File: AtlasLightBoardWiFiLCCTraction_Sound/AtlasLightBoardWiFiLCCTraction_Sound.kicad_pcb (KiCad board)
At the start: 2 copper layers, 76.7 x 20.3 mm, 47 parts, among them IC102 MP6614GN-Z, J101 USB_C_Receptacle, SW101 Reset, SW102 Boot, U101 ESP32_S3_WROOM, U102 TBD62083A, U103 AP63203WU

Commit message: Added I2S => Speaker chip (MAX98357A).
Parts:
- added TP105: Speaker, TestPoint:TestPoint_2Pads_Pitch2.54mm_Drill0.8mm, F.Cu at (133.4, 82.1)
- added U104: MAX98357AETE+T, Package_DFN_QFN:TQFN-16-1EP_3x3mm_P0.5mm_EP1.23x1.23mm_ThermalVias, F.Cu at (133.4, 78.7)
- moved U101 6.00 mm to (147.1, 78.7)
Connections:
- U101 pad 19: unconnected-(U101-Pad19) -> /I2S_TX
- U101 pad 20: unconnected-(U101-Pad20) -> /I2S_BCLK
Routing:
- net /I2S_TX: track 0.00 -> 7.90 mm, vias 0 -> 2
- net /D-: track 25.5 -> 33.3 mm
- net /D+: track 26.0 -> 33.7 mm
- net /Function2: track 73.9 -> 81.0 mm
- net /I2S_BCLK: track 0.00 -> 6.91 mm, vias 0 -> 2
- net +3V3: track 93.4 -> 99.8 mm
- net /Function3: track 75.0 -> 81.4 mm
- net /Reset: track 29.1 -> 35.4 mm
- net /MForward: track 54.6 -> 60.8 mm
- net /Function4: track 76.3 -> 82.4 mm
- net /MReverse: track 52.4 -> 58.4 mm
- net /Function5: track 74.3 -> 80.1 mm
- net GND: track 120.3 -> 126.0 mm
- net /Function6: track 87.6 -> 93.3 mm
- net Net-(TP105-Pad2): track 0.00 -> 3.79 mm
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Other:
- board size 76.7 x 20.3 mm -> 82.7 x 20.3 mm

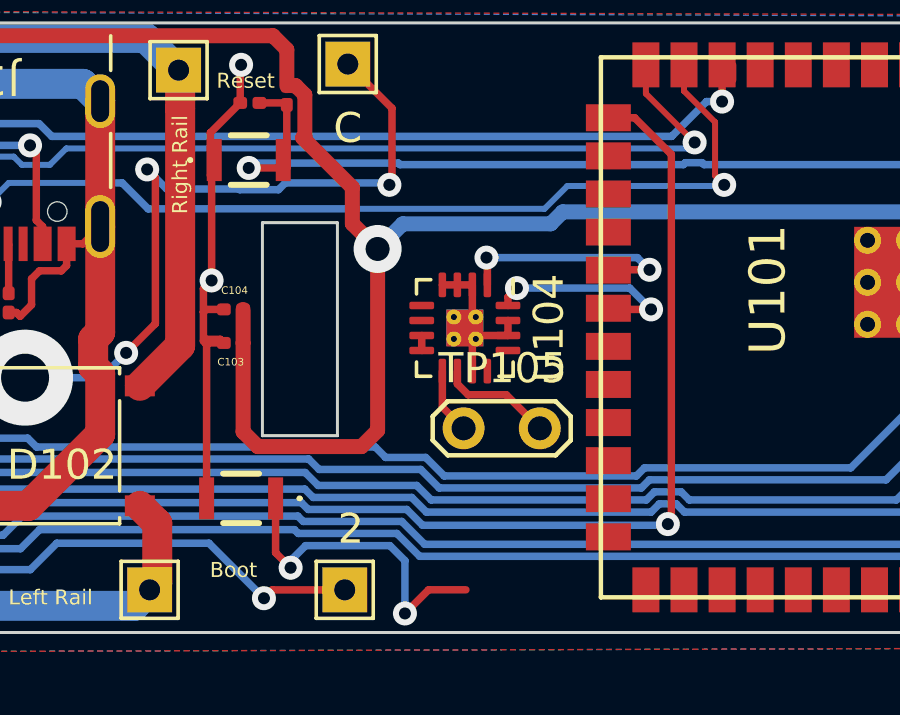
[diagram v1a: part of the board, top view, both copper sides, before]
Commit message: Added I2S => Speaker chip (MAX98357A).
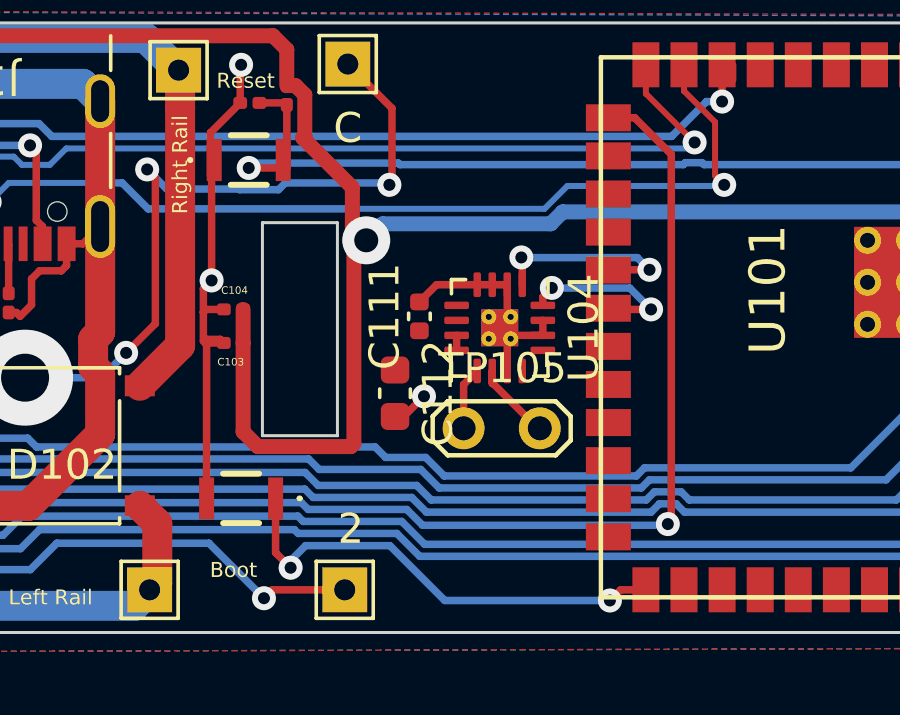
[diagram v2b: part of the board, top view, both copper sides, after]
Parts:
- added C111: .1uf, Capacitor_SMD:C_0402_1005Metric, F.Cu at (131.9, 78.4)
- added C112: 10 uf 6.3V, Capacitor_SMD:C_0603_1608Metric, F.Cu at (131.1, 80.9)
- moved U104 1.16 mm to (134.6, 78.7)
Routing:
- net /Boot0: track 11.1 -> 15.7 mm
- net GND: track 126.0 -> 129.4 mm, vias 5 -> 6
- net /I2S_TX: track 7.90 -> 6.74 mm
- net /I2S_BCLK: track 6.91 -> 5.75 mm
- net Net-(TP105-Pad2): track 3.79 -> 3.03 mm

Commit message: Update the doc/Images files.
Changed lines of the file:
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@@
     (property "Sheetname" "")
     (attr exclude_from_pos_files)
-    (fp_text reference "TP105" (at 1.3 -2) (layer "F.SilkS")
-      (effects (font (size 1 1) (thickness 0.15)))
-    )
-    (fp_text value "Speaker" (at 1.27 2) (layer "F.Fab")
+    (fp_text reference "TP105" (at 1.3 -2) (layer "F.Fab")
+      (effects (font (size 1 1) (thickness 0.15)))
+    )
+    (fp_text value "Speaker" (at 0.3556 1.9812) (layer "F.SilkS")
       (effects (font (size 1 1) (thickness 0.15)))
     )
@@
     (property "Sheetname" "")
     (attr smd)
-    (fp_text reference "C111" (at 0 -1.16 90) (layer "F.SilkS")
-      (effects (font (size 1 1) (thickness 0.15)))
+    (fp_text reference "C111" (at 0.0788 -0.9652 90) (layer "F.SilkS")
+      (effects (font (size 0.5 0.5) (thickness 0.075)))
     )
     (fp_text value ".1uf" (at 0 1.16 90) (layer "F.Fab")
@@
     (property "Sheetname" "")
     (attr smd)
-    (fp_text reference "C112" (at 0 -1.43 90) (layer "F.SilkS")
-      (effects (font (size 1 1) (thickness 0.15)))
+    (fp_text reference "C112" (at 0.254 1.2192 90) (layer "F.SilkS")
+      (effects (font (size 0.5 0.5) (thickness 0.075)))
     )
     (fp_text value "10 uf 6.3V" (at 0 1.43 90) (layer "F.Fab")
@@
     (property "Value_1" "MAX98357AETE+T")
     (attr smd)
-    (fp_text reference "U104" (at 0 -2.8 90) (layer "F.SilkS")
-      (effects (font (size 1 1) (thickness 0.15)))
+    (fp_text reference "U104" (at -0.258 -2.5043 90) (layer "F.SilkS")
+      (effects (font (size 0.5 0.5) (thickness 0.075)))
     )
     (fp_text value "MAX98357AETE+T" (at 0 2.8 90) (layer "F.Fab")
@@
     (pad "17" thru_hole circle (at -0.365 0.365 270) (size 0.5 0.5) (drill 0.2) (layers *.Cu)
       (net 2 "GND") (pinfunction "THERMAL_PAD") (pintype "passive"))
-    (model "${KICAD6_3DMODEL_DIR}/Package_DFN_QFN.3dshapes/TQFN-16-1EP_3x3mm_P0.5mm_EP1.23x1.23mm.wrl"
-      (offset (xyz 0 0 0))
-      (scale (xyz 1 1 1))
+    (model "${KICAD6_3DMODEL_DIR}/Package_DFN_QFN.3dshapes/QFN-16-1EP_3x3mm_P0.5mm_EP1.8x1.8mm.step"
+      (offset (xyz 0 0 0))
+      (scale (xyz 1 1 1))

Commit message: Add WS / LR Clock.
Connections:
- U101 pad 21: unconnected-(U101-Pad21) -> /LRCLK
- U104 pad 14: GND -> /LRCLK
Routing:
- net /LRCLK: track 0.00 -> 2.34 mm
- net GND: track 129.4 -> 128.8 mm
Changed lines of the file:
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@@
   (net 49 "Net-(TP105-Pad1)")
   (net 50 "Net-(TP105-Pad2)")
-  (net 51 "unconnected-(U101-Pad21)")
+  (net 51 "/LRCLK")
   (net 52 "unconnected-(U101-Pad22)")
   (net 53 "unconnected-(U101-Pad23)")
@@
       (net 71 "/I2S_BCLK") (pinfunction "IO12") (pintype "bidirectional"))
     (pad "21" smd rect locked (at 0.635 8.87 270) (size 0.9 1.5) (layers "F.Cu" "F.Paste" "F.Mask")
-      (net 51 "unconnected-(U101-Pad21)") (pinfunction "IO13") (pintype "bidirectional+no_connect"))
+      (net 51 "/LRCLK") (pinfunction "IO13") (pintype "bidirectional"))
     (pad "22" smd rect locked (at 1.905 8.87 270) (size 0.9 1.5) (layers "F.Cu" "F.Paste" "F.Mask")
       (net 52 "unconnected-(U101-Pad22)") (pinfunction "IO14") (pintype "bidirectional+no_connect"))
@@
       (net 76 "unconnected-(U104-Pad13)") (pinfunction "N.C._4") (pintype "passive+no_connect"))
     (pad "14" smd roundrect (at 0.25 -1.4375 270) (size 0.25 0.825) (layers "F.Cu" "F.Paste" "F.Mask") (roundrect_rratio 0.25)
-      (net 2 "GND") (pinfunction "LRCLK") (pintype "passive"))
+      (net 51 "/LRCLK") (pinfunction "LRCLK") (pintype "passive"))
     (pad "15" smd roundrect (at -0.25 -1.4375 270) (size 0.25 0.825) (layers "F.Cu" "F.Paste" "F.Mask") (roundrect_rratio 0.25)
       (net 2 "GND") (pinfunction "GND_3") (pintype "passive"))
@@
   (segment (start 121.052287 80.03442) (end 121.287 80.269133) (width 1) (layer "F.Cu") (net 2))
   (segment (start 103.403 74.168) (end 103.378 74.168) (width 0.25) (layer "F.Cu") (net 2))
-  (segment (start 136.0424 78.994) (end 134.8549 78.994) (width 0.25) (layer "F.Cu") (net 2))
   (segment (start 107.569 77.535) (end 107.442 77.662) (width 0.25) (layer "F.Cu") (net 2))
-  (segment (start 136.0424 78.494) (end 136.0424 78.994) (width 0.25) (layer "F.Cu") (net 2))
   (segment (start 131.4066 81.6994) (end 132.08 81.026) (width 0.25) (layer "F.Cu") (net 2))
   (segment (start 124.834 79.128) (end 125.29 79.128) (width 0.25) (layer "F.Cu") (net 2))
@@
   (segment (start 92.362 80.805) (end 92.329 80.772) (width 0.25) (layer "F.Cu") (net 2))
   (segment (start 118.999 77.978) (end 118.999 77.111) (width 0.25) (layer "F.Cu") (net 2))
+  (segment (start 135.0849 78.494) (end 134.9699 78.379) (width 0.25) (layer "F.Cu") (net 2))
   (segment (start 108.585 76.454) (end 106.68 78.359) (width 0.25) (layer "F.Cu") (net 2))
   (segment (start 124.8156 78.1304) (end 124.727 78.219) (width 0.25) (layer "F.Cu") (net 2))
   (segment (start 133.8549 77.3065) (end 134.3549 77.3065) (width 0.25) (layer "F.Cu") (net 2))
+  (segment (start 136.0424 78.494) (end 135.0849 78.494) (width 0.25) (layer "F.Cu") (net 2))
   (segment (start 113.767 75.943) (end 113.222 75.943) (width 0.25) (layer "F.Cu") (net 2))
   (segment (start 119.267 76.843) (end 119.992 76.843) (width 0.25) (layer "F.Cu") (net 2))
@@
   (segment (start 134.3549 80.1815) (end 134.3549 80.6088) (width 0.25) (layer "F.Cu") (net 50))
   (segment (start 135.876403 82.0928) (end 135.9408 82.0928) (width 0.25) (layer "F.Cu") (net 50))
+  (segment (start 136.0424 78.994) (end 137.859 78.994) (width 0.25) (layer "F.Cu") (net 51))
+  (segment (start 137.859 78.994) (end 138.227 79.362) (width 0.25) (layer "F.Cu") (net 51))
   (segment (start 92.5068 73.751101) (end 92.5068 73.688) (width 0.25) (layer "F.Cu") (net 69))
   (segment (start 91.643 75.847) (end 91.643 74.614901) (width 0.25) (layer "F.Cu") (net 69))

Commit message: Minor tweaks: MONO mode resister, trace symblification.
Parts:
- added R111: 634k, Resistor_SMD:R_0402_1005Metric, F.Cu at (133.3, 76.0)
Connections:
- U104 pad 4: GND -> Net-(U104-Pad4)
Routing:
- net /I2S_TX: track 6.74 -> 3.09 mm, vias 2 -> 0
- net /I2S_BCLK: track 5.75 -> 2.28 mm, vias 2 -> 0
- net GND: track 128.8 -> 127.1 mm, vias 6 -> 7
- net Net-(U104-Pad4): track 0.00 -> 1.33 mm
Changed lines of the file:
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@@
   (net 75 "unconnected-(U104-Pad12)")
   (net 76 "unconnected-(U104-Pad13)")
+  (net 77 "Net-(U104-Pad4)")
   (footprint "TestPoint:TestPoint_THTPad_1.5x1.5mm_Drill0.7mm" (layer "F.Cu")
     (at 122.936 87.4776)
@@
       (net 21 "Net-(R103-Pad1)") (pinfunction "1") (pintype "passive"))
   )
+  (footprint "Resistor_SMD:R_0402_1005Metric" (layer "F.Cu")
+    (at 133.2992 75.9968)
+    (descr "Resistor SMD 0402 (1005 Metric), square (rectangular) end terminal, IPC_7351 nominal, (Body size source: IPC-SM-782 page 72, https://www.pcb-3d.com/wordpress/wp-content/uploads/ipc-sm-782a_amendment_1_and_2.pdf), generated with kicad-footprint-generator")
+    (tags "resistor")
+    (property "Sheetfile" "AtlasLightBoardWiFiLCCTraction_Sound.kicad_sch")
+    (property "Sheetname" "")
+    (attr smd)
+    (fp_text reference "R111" (at 0 -1.17) (layer "F.SilkS")
+      (effects (font (size 1 1) (thickness 0.15)))
+    )
+    (fp_text value "634k" (at 0 1.17) (layer "F.Fab")
+      (effects (font (size 1 1) (thickness 0.15)))
+    )
+    (fp_text user "${REFERENCE}" (at 0 0) (layer "F.Fab")
+      (effects (font (size 0.26 0.26) (thickness 0.04)))
+    )
+    (fp_line (start -0.153641 0.38) (end 0.153641 0.38) (layer "F.SilkS") (width 0.12))
+    (fp_line (start -0.153641 -0.38) (end 0.153641 -0.38) (layer "F.SilkS") (width 0.12))
+    (fp_line (start -0.93 -0.47) (end 0.93 -0.47) (layer "F.CrtYd") (width 0.05))
+    (fp_line (start 0.93 0.47) (end -0.93 0.47) (layer "F.CrtYd") (width 0.05))
+    (fp_line (start -0.93 0.47) (end -0.93 -0.47) (layer "F.CrtYd") (width 0.05))
+    (fp_line (start 0.93 -0.47) (end 0.93 0.47) (layer "F.CrtYd") (width 0.05))
+    (fp_line (start 0.525 -0.27) (end 0.525 0.27) (layer "F.Fab") (width 0.1))
+    (fp_line (start 0.525 0.27) (end -0.525 0.27) (layer "F.Fab") (width 0.1))
+    (fp_line (start -0.525 0.27) (end -0.525 -0.27) (layer "F.Fab") (width 0.1))
+    (fp_line (start -0.525 -0.27) (end 0.525 -0.27) (layer "F.Fab") (width 0.1))
+    (pad "1" smd roundrect (at -0.51 0) (size 0.54 0.64) (layers "F.Cu" "F.Paste" "F.Mask") (roundrect_rratio 0.25)
+      (net 4 "+3V3") (pintype "passive"))
+    (pad "2" smd roundrect (at 0.51 0) (size 0.54 0.64) (layers "F.Cu" "F.Paste" "F.Mask") (roundrect_rratio 0.25)
+      (net 77 "Net-(U104-Pad4)") (pintype "passive"))
+    (model "${KICAD6_3DMODEL_DIR}/Resistor_SMD.3dshapes/R_0402_1005Metric.wrl"
+      (offset (xyz 0 0 0))
+      (scale (xyz 1 1 1))
+      (rotate (xyz 0 0 0))
+    )
+  )
   (footprint "Connector_USB:USB_C_Receptacle_GCT_USB4105-xx-A_16P_TopMnt_Horizontal" (layer "F.Cu")
     (at 116.967 72.263 180)
@@
       (net 2 "GND") (pinfunction "GND_1") (pintype "passive"))
     (pad "4" smd roundrect (at -1.4375 0.75 270) (size 0.825 0.25) (layers "F.Cu" "F.Paste" "F.Mask") (roundrect_rratio 0.25)
-      (net 2 "GND") (pinfunction "~{SD_MODE}") (pintype "passive"))
+      (net 77 "Net-(U104-Pad4)") (pinfunction "~{SD_MODE}") (pintype "passive"))
     (pad "5" smd roundrect (at -0.75 1.4375 270) (size 0.25 0.825) (layers "F.Cu" "F.Paste" "F.Mask") (roundrect_rratio 0.25)
       (net 73 "unconnected-(U104-Pad5)") (pinfunction "N.C._1") (pintype "passive+no_connect"))
@@
   (segment (start 125.984 69.977) (end 125.954 70.007) (width 0.25) (layer "F.Cu") (net 2))
   (segment (start 155.987 87.477) (end 155.987 69.977) (width 0.25) (layer "F.Cu") (net 2))
-  (segment (start 132.5027 77.3065) (end 131.9276 77.8816) (width 0.25) (layer "F.Cu") (net 2))
   (segment (start 115.189 78.207) (end 114.148 78.207) (width 0.25) (layer "F.Cu") (net 2))
   (segment (start 114.148 78.207) (end 113.767 77.826) (width 0.25) (layer "F.Cu") (net 2))
@@
   (segment (start 113.792 85.316) (end 116.02 85.316) (width 1) (layer "F.Cu") (net 2))
   (segment (start 118.492 78.233) (end 118.618 78.359) (width 0.25) (layer "F.Cu") (net 2))
+  (segment (start 131.9276 77.0636) (end 131.8768 77.0128) (width 0.25) (layer "F.Cu") (net 2))
   (segment (start 113.222 75.943) (end 112.647 75.368) (width 0.25) (layer "F.Cu") (net 2))
   (segment (start 91.326 73.770579) (end 89.023579 76.073) (width 1) (layer "F.Cu") (net 2))
@@
   (segment (start 118.895402 84.677) (end 116.659 84.677) (width 1) (layer "F.Cu") (net 2))
   (segment (start 125.954 70.007) (end 125.954 71.247) (width 0.25) (layer "F.Cu") (net 2))
-  (segment (start 133.8549 77.3065) (end 132.5027 77.3065) (width 0.25) (layer "F.Cu") (net 2))
   (segment (start 101.727 75.819) (end 101.727 72.771) (width 1) (layer "F.Cu") (net 2))
   (segment (start 121.287 75.368) (end 121.287 78.888437) (width 1) (layer "F.Cu") (net 2))
@@
   (segment (start 108.585 76.454) (end 106.68 78.359) (width 0.25) (layer "F.Cu") (net 2))
   (segment (start 124.8156 78.1304) (end 124.727 78.219) (width 0.25) (layer "F.Cu") (net 2))
-  (segment (start 133.8549 77.3065) (end 134.3549 77.3065) (width 0.25) (layer "F.Cu") (net 2))
+  (segment (start 131.9276 77.8816) (end 131.9276 77.0636) (width 0.25) (layer "F.Cu") (net 2))
   (segment (start 136.0424 78.494) (end 135.0849 78.494) (width 0.25) (layer "F.Cu") (net 2))
   (segment (start 113.767 75.943) (end 113.222 75.943) (width 0.25) (layer "F.Cu") (net 2))
@@
   (via (at 132.08 81.026) (size 0.8) (drill 0.4) (layers "F.Cu" "B.Cu") (net 2))
   (via (at 125.984 69.977) (size 0.8) (drill 0.4) (layers "F.Cu" "B.Cu") (net 2))
+  (via (at 131.8768 77.0128) (size 0.8) (drill 0.4) (layers "F.Cu" "B.Cu") (net 2))
   (via (at 88.646 76.073) (size 3.2) (drill 1.6) (layers "F.Cu" "B.Cu") (net 2))
   (segment (start 113.223 70.612) (end 112.647 71.188) (width 1) (layer "B.Cu") (net 2))
@@
   (segment (start 93.8205 74.648) (end 94.1125 74.356) (width 0.25) (layer "F.Cu") (net 70))
   (segment (start 92.5068 74.648) (end 93.8205 74.648) (width 0.25) (layer "F.Cu") (net 70))
-  (segment (start 136.0424 77.7129) (end 136.3415 77.4138) (width 0.25) (layer "F.Cu") (net 71))
+  (segment (start 136.0424 77.994) (end 138.129 77.994) (width 0.25) (layer "F.Cu") (net 71))
+  (segment (start 138.129 77.994) (end 138.227 78.092) (width 0.25) (layer "F.Cu") (net 71))
   (segment (start 138.2654 78.1304) (end 138.227 78.092) (width 0.25) (layer "F.Cu") (net 71))
-  (segment (start 139.6492 78.1304) (end 138.2654 78.1304) (width 0.25) (layer "F.Cu") (net 71))
-  (segment (start 136.0424 77.994) (end 136.0424 77.7129) (width 0.25) (layer "F.Cu") (net 71))
-  (via (at 136.3415 77.4138) (size 0.8) (drill 0.4) (layers "F.Cu" "B.Cu") (net 71))
-  (via (at 139.6492 78.1304) (size 0.8) (drill 0.4) (layers "F.Cu" "B.Cu") (net 71))
-  (segment (start 136.3469 77.4192) (end 136.3415 77.4138) (width 0.25) (layer "B.Cu") (net 71))
-  (segment (start 138.938 77.4192) (end 136.3469 77.4192) (width 0.25) (layer "B.Cu") (net 71))
-  (segment (start 139.6492 78.1304) (end 138.938 77.4192) (width 0.25) (layer "B.Cu") (net 71))
-  (segment (start 139.5984 76.8096) (end 138.2394 76.8096) (width 0.25) (layer "F.Cu") (net 72))
+  (segment (start 135.3549 77.3065) (end 135.8394 76.822) (width 0.25) (layer "F.Cu") (net 72))
   (segment (start 138.2394 76.8096) (end 138.227 76.822) (width 0.25) (layer "F.Cu") (net 72))
-  (segment (start 135.3549 76.4272) (end 135.3255 76.3978) (width 0.25) (layer "F.Cu") (net 72))
-  (segment (start 135.3549 77.3065) (end 135.3549 76.4272) (width 0.25) (layer "F.Cu") (net 72))
-  (via (at 135.3255 76.3978) (size 0.8) (drill 0.4) (layers "F.Cu" "B.Cu") (net 72))
-  (via (at 139.5984 76.8096) (size 0.8) (drill 0.4) (layers "F.Cu" "B.Cu") (net 72))
-  (segment (start 135.3309 76.4032) (end 135.3255 76.3978) (width 0.25) (layer "B.Cu") (net 72))
-  (segment (start 139.192 76.4032) (end 135.3309 76.4032) (width 0.25) (layer "B.Cu") (net 72))
-  (segment (start 139.5984 76.8096) (end 139.192 76.4032) (width 0.25) (layer "B.Cu") (net 72))
+  (segment (start 135.8394 76.822) (end 138.227 76.822) (width 0.25) (layer "F.Cu") (net 72))
+  (segment (start 133.8549 77.3065) (end 133.8549 76.0425) (width 0.25) (layer "F.Cu") (net 77))
+  (segment (start 133.8549 76.0425) (end 133.8092 75.9968) (width 0.25) (layer "F.Cu") (net 77))
   (zone (net 4) (net_name "+3V3") (layer "F.Cu") (hatch edge 0.508)
     (connect_pads yes (clearance 0.508))
